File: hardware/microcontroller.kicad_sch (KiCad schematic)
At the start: 12 parts, among them J1 AVR-ISP-6, SW2 SKRPACE010, U1 ATmega328P-A, Y2 Crystal-32kHz

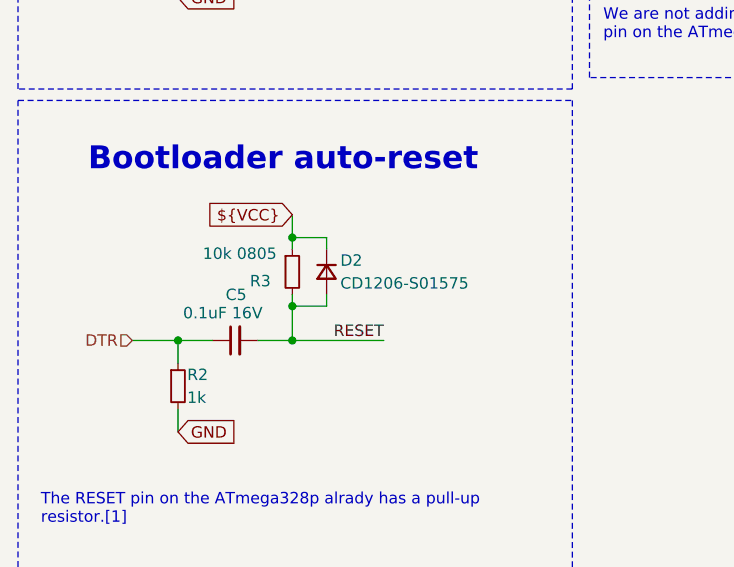
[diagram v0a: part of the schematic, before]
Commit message: Added many footprints and populated part of the property tables
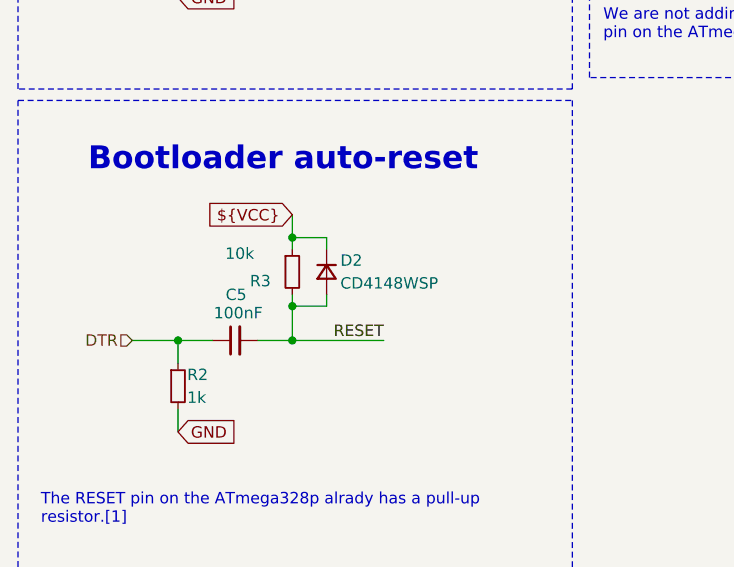
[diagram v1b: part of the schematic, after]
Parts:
- C1, C2: footprint (none) -> Capacitor_SMD:C_0805_2012Metric_Pad1.18x1.45mm_HandSolder; Manuf. Name (none) -> Murata Electronics; Manuf. Part # (none) -> GRM21BR71H104KA01L; Package (none) -> 0805; Supplier Link (none) -> https://jlcpcb.com/partdetail/MurataElectronics-GRM21BR71H1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; Supplier Name (none) -> JLCPCB; Supplier Part # (none) -> C77082; Supplier Unit Price (none) -> $0.0099
- C3, C4: footprint (none) -> Capacitor_SMD:C_0805_2012Metric_Pad1.18x1.45mm_HandSolder; Manuf. Name (none) -> Samsung Electro-Mechanics; Manuf. Part # (none) -> CL21C220JBANNNC; Package (none) -> 0805; Supplier Link (none) -> https://jlcpcb.com/partdetail/2156-CL21C220JBANNNC/C1804; Supplier Name (none) -> JLCPCB; Supplier Part # (none) -> C1804; Supplier Unit Price (none) -> $0.0094
- C5: value 0.1uF 16V -> 100nF; footprint (none) -> Capacitor_SMD:C_0805_2012Metric_Pad1.18x1.45mm_HandSolder; Manuf. Name (none) -> Murata Electronics; Supplier Link https://jlcpcb.com/partdetail/MurataElectronics-GRM21BR71H104KA01L/C77082 -> https://jlcpcb.com/partdetail/MurataElectronics-GRM21BR71H104KA01L/C77082; Supplier Part # (none) -> C77082; Supplier Unit Price $0.0097 -> $0.0099
- D2: value CD1206-S01575 -> CD4148WSP; footprint (none) -> Diode_SMD:D_0805_2012Metric; Manuf. Name (none) -> LIZ Elec; Manuf. Part # (none) -> CD4148WSP; Package (none) -> 0805; Supplier Link (none) -> https://jlcpcb.com/partdetail/LizElec-CD4148WSP/C109001; Supplier Name (none) -> JLCPCB; Supplier Part # (none) -> C109001; Supplier Unit Price (none) -> $0.0117
- J1: footprint (none) -> Connector_PinHeader_2.54mm:PinHeader_2x03_P2.54mm_Vertical; now left out of the parts list
- R2: footprint (none) -> Resistor_SMD:R_0805_2012Metric_Pad1.20x1.40mm_HandSolder; Manuf. Name (none) -> UNI-ROYAL(Uniroyal Elec); Manuf. Part # (none) -> 0805W8F1001T5E; Package (none) -> 0805; Supplier Link (none) -> https://jlcpcb.com/partdetail/18201-0805W8F1001T5E/C17513; Supplier Name (none) -> JLCPCB; Supplier Part # (none) -> C17513; Supplier Unit Price (none) -> $0.0017
- R3: value 10k 0805 -> 10k; footprint (none) -> Resistor_SMD:R_0805_2012Metric_Pad1.20x1.40mm_HandSolder; Manuf. Name (none) -> UNI-ROYAL(Uniroyal Elec); Supplier Part # (none) -> C17414
- SW2: footprint (none) -> kitchen_timer:SW_SKRPACE010; Supplier Part # (none) -> C139797; Supplier Unit Price $0.0573 -> $0.0638

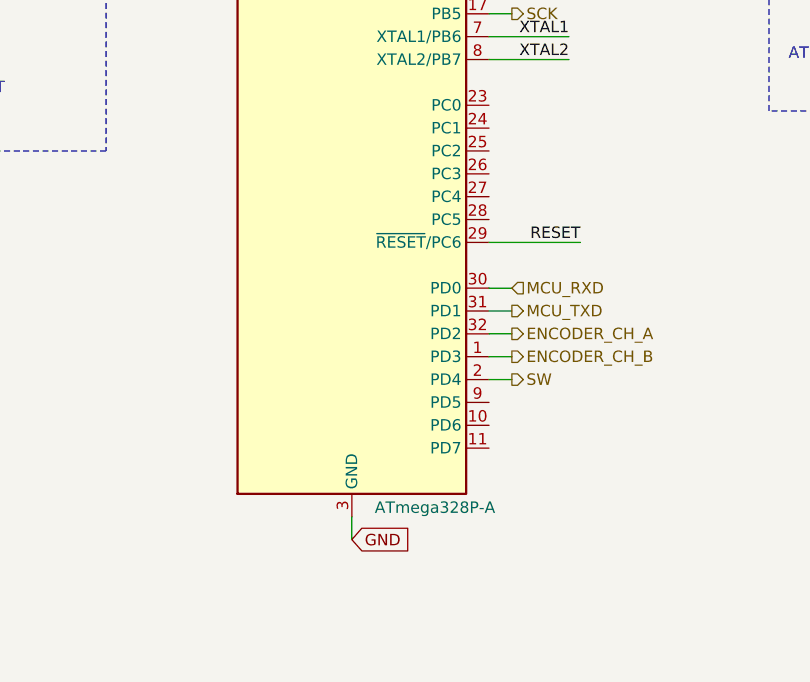
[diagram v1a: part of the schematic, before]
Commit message: Completed the property teble except for the cyristal oscilator
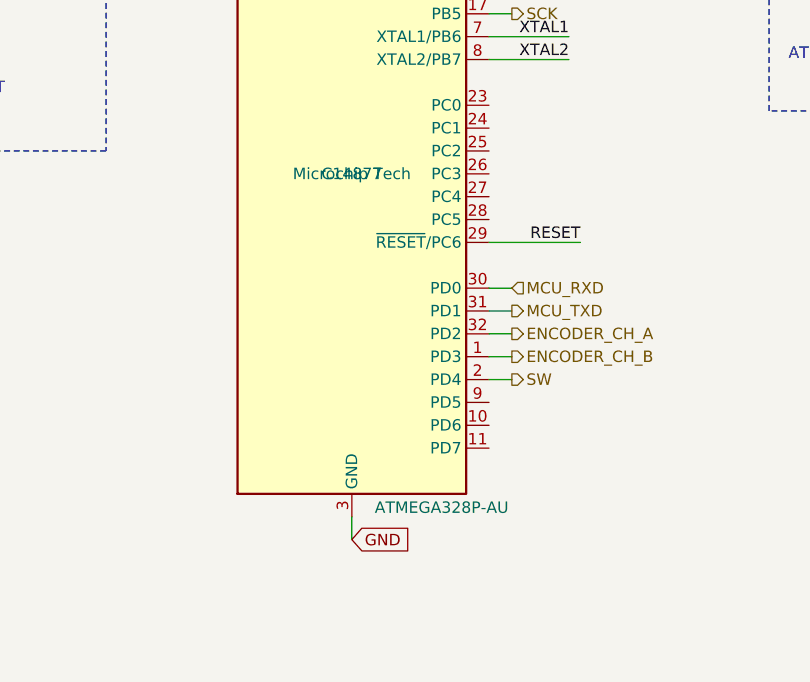
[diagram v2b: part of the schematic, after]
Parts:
- U1: value ATmega328P-A -> ATMEGA328P-AU; Manuf. Name (none) -> Microchip Tech; Supplier Part # (none) -> C14877; Supplier Unit Price $2.2845 -> $2.5905
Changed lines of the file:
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@@
 			)
 		)
-		(property "Description" "Resistor, small symbol"
+		(property "Description" "10k, 0805"
 			(at 46.99 118.11 0)
 			(effects
@@
 			)
 		)
-		(property "Value" "ATmega328P-A"
+		(property "Value" "ATMEGA328P-AU"
 			(at 171.45 136.144 0)
 			(effects
@@
 			)
 		)
-		(property "Datasheet" "https://drive.google.com/drive/folders/1J5PdYHZlJh-48GetU7TEXl5JsmDgvT0e"
-			(at 168.91 99.06 0)
-			(effects
-				(font
-					(size 1.27 1.27)
-				)
-				(hide yes)
-			)
-		)
-		(property "Description" "20MHz, 32kB Flash, 2kB SRAM, 1kB EEPROM, TQFP-32"
+		(property "Datasheet" "https://jlcpcb.com/api/file/downloadByFileSystemAccessId/8586171945553838081"
+			(at 168.91 99.06 0)
+			(effects
+				(font
+					(size 1.27 1.27)
+				)
+				(hide yes)
+			)
+		)
+		(property "Description" "32KB 2KB FLASH 23 1.8V~5.5V AVR 20MHz TQFP-32(7x7) Microcontrollers (MCU/MPU/SOC) ROHS"
 			(at 168.91 99.06 0)
 			(effects
@@
 			)
 		)
-		(property "Supplier Unit Price" "$2.2845"
+		(property "Supplier Unit Price" "$2.5905"
 			(at 168.402 92.964 0)
 			(effects
@@
 			)
 		)
+		(property "Manuf. Name" "Microchip Tech"
+			(at 168.91 99.06 0)
+			(effects
+				(font
+					(size 1.27 1.27)
+				)
+			)
+		)
+		(property "Supplier Part #" "C14877"
+			(at 168.91 99.06 0)
+			(effects
+				(font
+					(size 1.27 1.27)
+				)
+			)
+		)

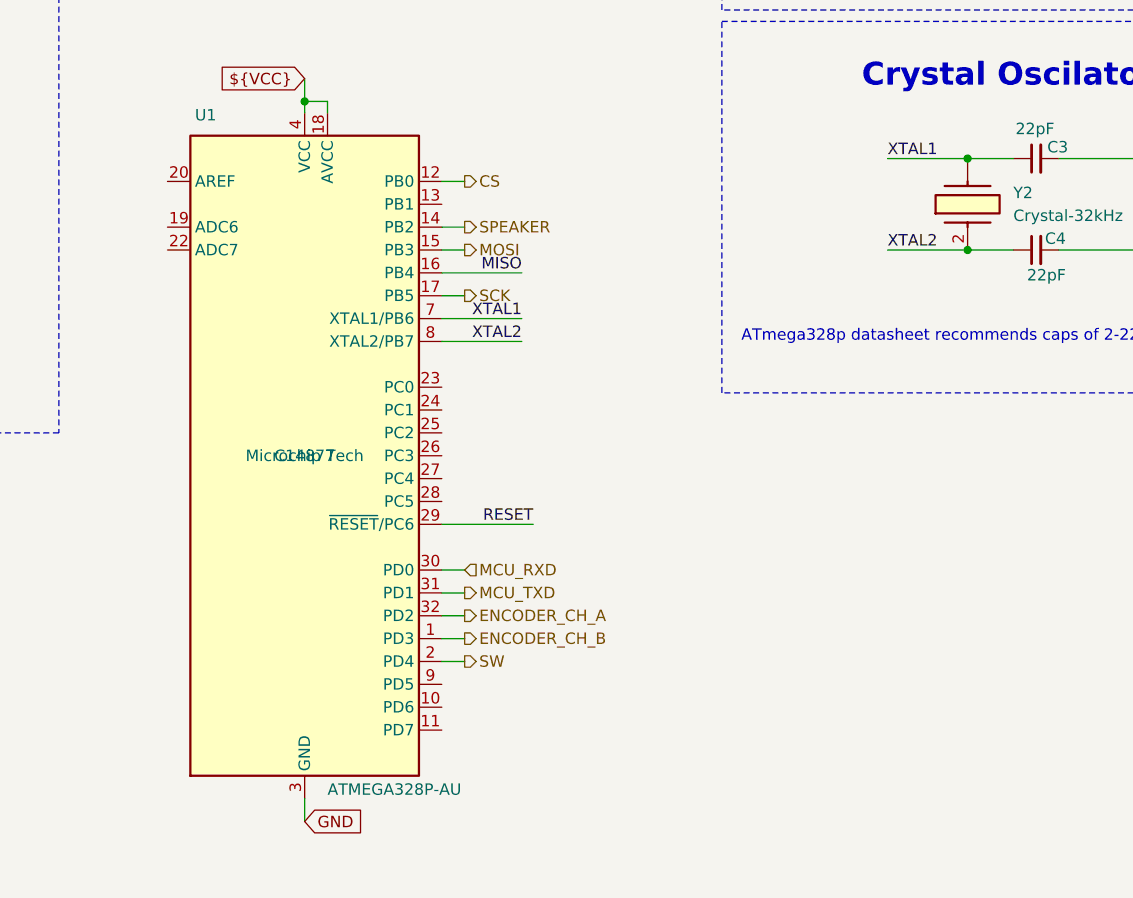
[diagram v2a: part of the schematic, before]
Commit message: Made some small changes on the properties of some components while having last weeks meeting and added the fp-info-cache to the gitignore file
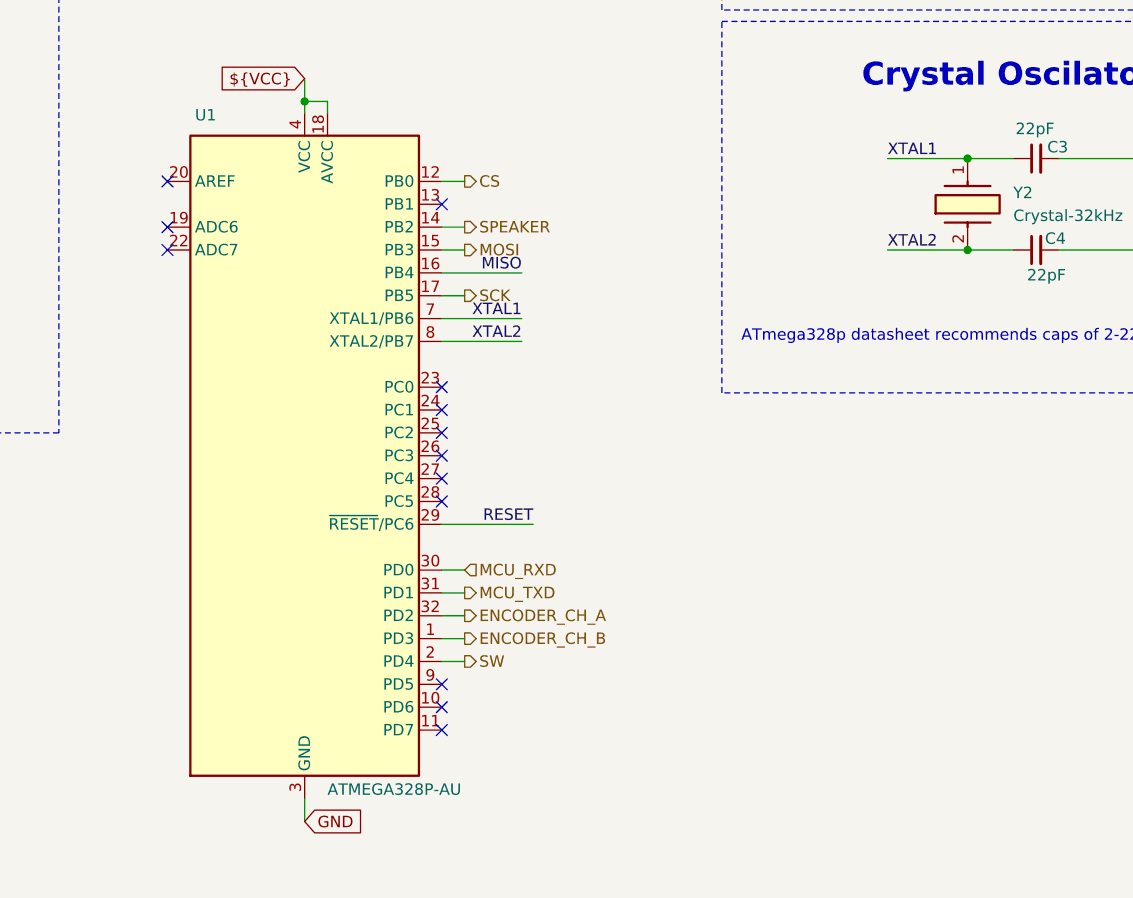
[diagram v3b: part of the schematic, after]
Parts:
- Y2: Manuf. Name HCI -> Multitech; Supplier Link https://jlcpcb.com/parts/1st/Crystals_Oscillators_Resonator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 -> (none); Supplier Name JLCPCB -> (none); Supplier Unit Price $0.2669 -> (none); now left out of the parts list
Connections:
- net XTAL1: now also Y2.1; no longer Y2.
- no-connect marks 0 -> 13
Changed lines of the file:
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@@
 		(color 0 0 0 0)
+	)
+	(no_connect
+		(at 184.15 129.54)
+	)
+	(no_connect
+		(at 184.15 99.06)
+	)
+	(no_connect
+		(at 184.15 71.12)
+	)
+	(no_connect
+		(at 153.67 76.2)
+	)
+	(no_connect
+		(at 184.15 127)
+	)
+	(no_connect
+		(at 153.67 68.58)
+	)
+	(no_connect
+		(at 153.67 73.66)
+	)
+	(no_connect
+		(at 184.15 91.44)
+	)
+	(no_connect
+		(at 184.15 104.14)
+	)
+	(no_connect
+		(at 184.15 101.6)
+	)
+	(no_connect
+		(at 184.15 93.98)
+	)
+	(no_connect
+		(at 184.15 96.52)
+	)
+	(no_connect
+		(at 184.15 124.46)
 	)
 	(wire
@@
 		(unit 1)
 		(exclude_from_sim no)
-		(in_bom yes)
+		(in_bom no)
 		(on_board yes)
 		(dnp no)
@@
 			)
 		)
-		(property "Supplier Link" "https://jlcpcb.com/parts/1st/Crystals_Oscillators_Resonators_7"
+		(property "Supplier Link" "~"
 			(at 242.57 76.2 0)
 			(effects
@@
 			)
 		)
-		(property "Manuf. Name" "HCI"
+		(property "Manuf. Name" "Multitech"
 			(at 242.57 76.2 0)
 			(effects
@@
 			)
 		)
-		(property "Supplier Name" "JLCPCB"
+		(property "Supplier Name" "~"
 			(at 242.57 76.2 0)
 			(effects
@@
 			)
 		)
-		(property "Supplier Unit Price" " $0.2669"
+		(property "Supplier Unit Price" "~"
 			(at 242.57 76.2 0)
 			(effects
@@
 			)
 		)
+		(property "Supplier Part #" "~"
+			(at 242.57 76.2 0)
+			(effects
+				(font
+					(size 1.27 1.27)
+				)
+			)
+		)
 		(pin "2"
 		)
-		(pin ""
+		(pin "1"
 		)
 		(instances
@@
 			)
 		)
-		(property "Datasheet" "https://jlcpcb.com/api/file/downloadByFileSystemAccessId/8586171945553838081"
+		(property "Datasheet" "https://ww1.microchip.com/downloads/en/DeviceDoc/Atmel-7810-Automotive-Microcontrollers-ATmega328P_Datasheet.pdf"
 			(at 168.91 99.06 0)
 			(effects
@@
 					(size 1.27 1.27)
 				)
+				(hide yes)
 			)
 		)
@@
 					(size 1.27 1.27)
 				)
-			)
-		)
+				(hide yes)
+			)
+		)
+		(property "Part Num" ""
+			(at 168.91 99.06 0)
+			(effects
+				(font
+					(size 1.27 1.27)
+				)
+				(hide yes)
+			)
+		)

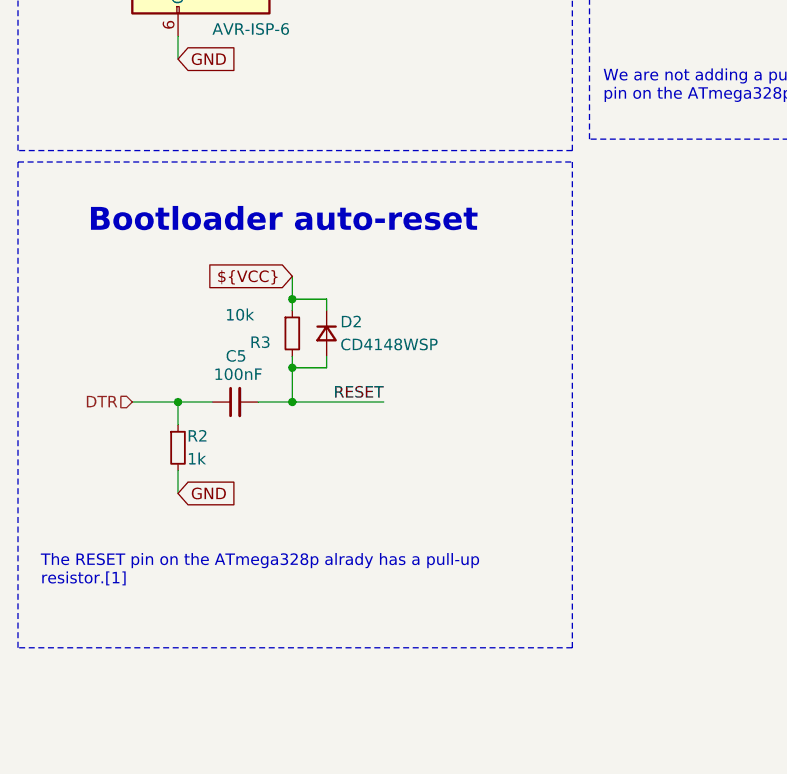
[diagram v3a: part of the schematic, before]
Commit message: Removed the extra components on the bootloader auto-reset
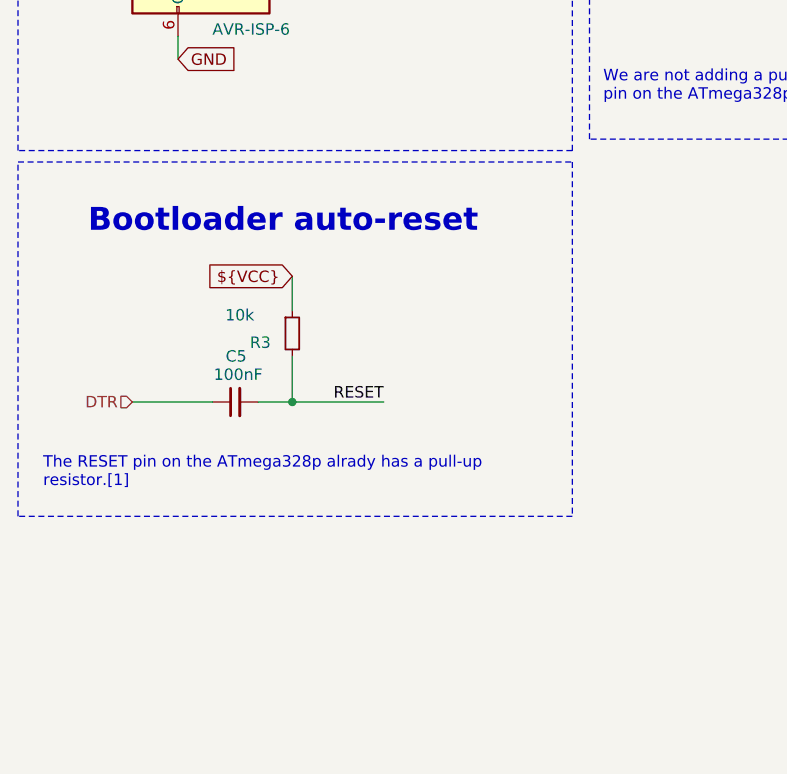
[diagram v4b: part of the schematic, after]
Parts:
- removed D2: CD4148WSP, Diode_SMD:D_0805_2012Metric, symbol Device:D_Small
- removed R2: 1k, Resistor_SMD:R_0805_2012Metric_Pad1.20x1.40mm_HandSolder, symbol Device:R_Small

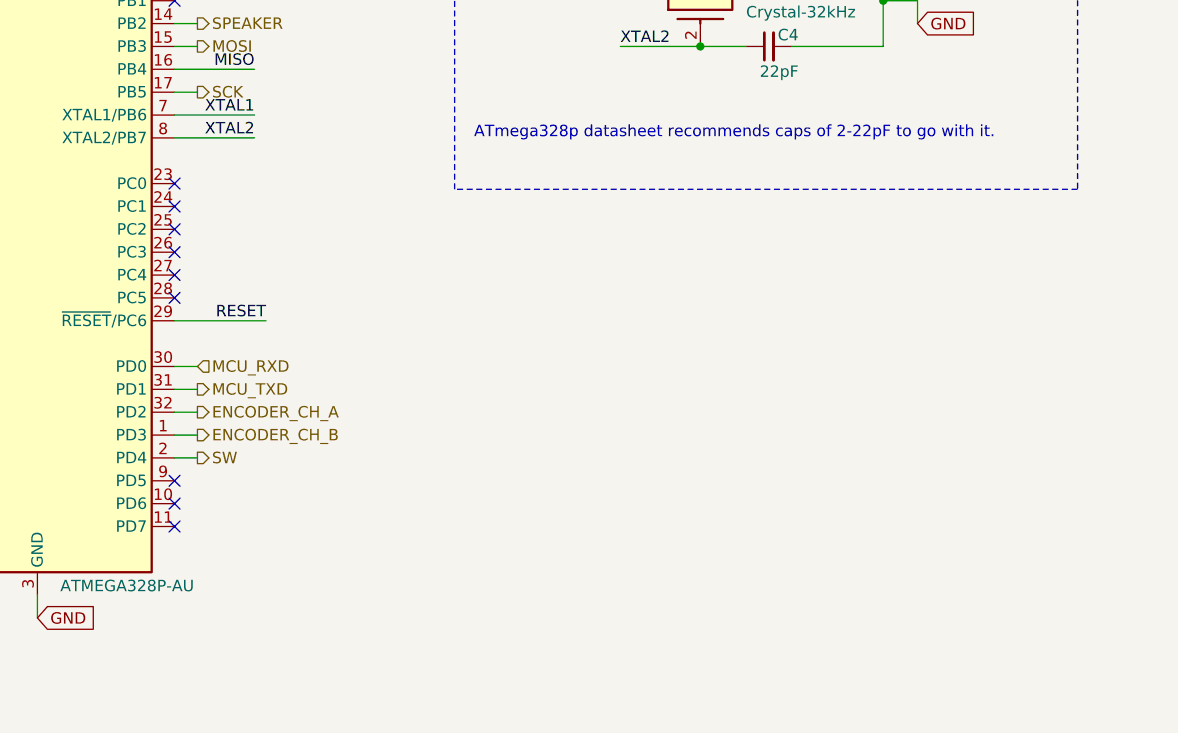
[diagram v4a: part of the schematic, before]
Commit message: Added a test LED to pin PC0
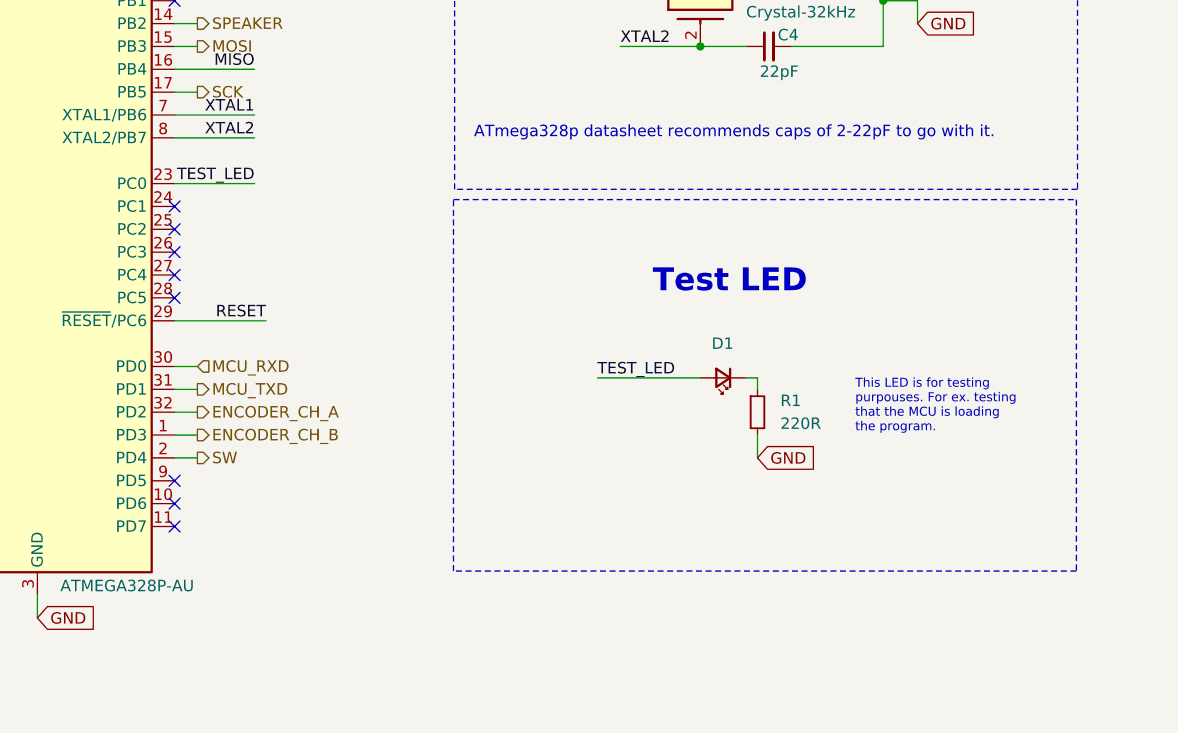
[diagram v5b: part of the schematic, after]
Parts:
- added D1: LED_Small, symbol Device:LED_Small
- added R1: 220R, symbol Device:R_Small
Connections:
- net GND: now also R1.2
- net TEST_LED: now reaches U1.23 (PC0)
- net TEST_LED: now also D1.2 (A)
- new net: D1.1 (K), R1.1
- no-connect marks 13 -> 12
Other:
- note added: "Test LED"
